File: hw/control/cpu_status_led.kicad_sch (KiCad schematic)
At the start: 4 parts, among them Q701 BC817

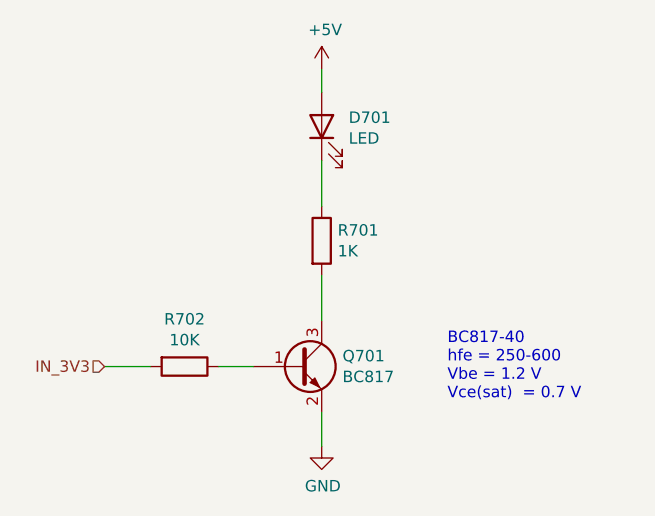
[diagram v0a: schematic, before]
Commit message: [hw] Update to KiCAD 7
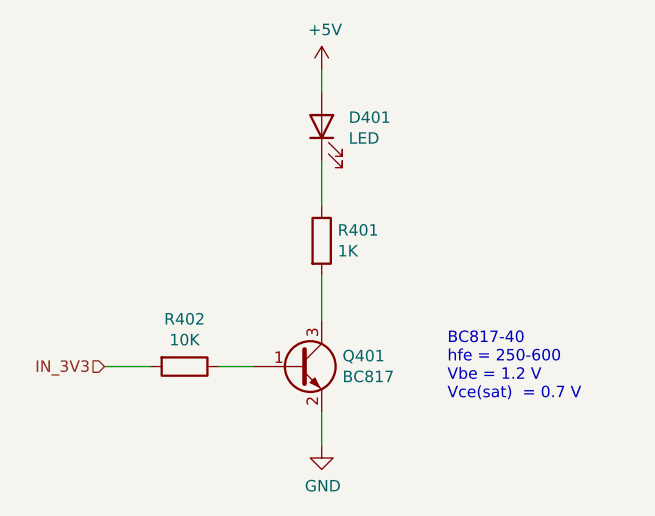
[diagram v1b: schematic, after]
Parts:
- renumbered D701 to D401, Q701 to Q401, R701 to R401, R702 to R402
